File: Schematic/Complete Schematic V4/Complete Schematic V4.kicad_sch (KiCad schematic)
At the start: 62 parts

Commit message: New Update
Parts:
- removed R?: 50, symbol Device:R
- C1, C4: renamed from C?; value 270p -> (none)
- C10, C11, C12, C9: renamed from C?; value 0.22u -> (none)
- C13, C26, C27: renamed from C?; value 10u -> (none)
- C14, C15, C18, C21, C24, C25, C3, C5, C6: renamed from C?; value 0.1u -> (none)
- C16, C17, C7: renamed from C?; value 10n -> (none)
- C19, C20: renamed from C?; value 105p -> (none)
- C2: renamed from C?; value 560p -> (none)
- C22, C23: renamed from C?; value 100p -> (none)
- C8: renamed from C?; value 100n -> (none)
- J1: renamed from J?; footprint (none) -> Connector_Coaxial:BNC_Amphenol_B6252HB-NPP3G-50_Horizontal
- L1, L3: renamed from L?; value 750n -> (none)
- L2: renamed from L?; value 360n -> (none)
- R10, R11: renamed from R?; value 4.64k -> (none)
- R12, R13: renamed from R?; value 52.3k -> (none)
- R14, R15: renamed from R?; value 2.49k -> (none)
- R16, R17: renamed from R?; value 17.4k -> (none)
- R18, R19: renamed from R?; value 4.7k -> (none)
- R20, R21: renamed from R?; value 100 -> (none)
- R3: renamed from R?; value 10k -> (none)
- R4, R5, R6, R7: renamed from R?; value 200 -> (none)
- R8, R9: renamed from R?; value 22k -> (none)
- U1: renamed from U?; footprint Package_SO:MSOP-10_3x3mm_P0.5mm -> (none)
- U3, U4: renamed from U?; value OPAMP -> LT6231; footprint (none) -> Package_SO:SOIC-8_3.9x4.9mm_P1.27mm
- U5, U6: renamed from U?; value OPAMP -> LM4562MA; footprint (none) -> Package_SO:SOIC-8_3.9x4.9mm_P1.27mm
- gave numbers to parts that had none: 6
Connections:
- net at C1.2: now also J1.2 (Ext)
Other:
- moved on the sheet: C18

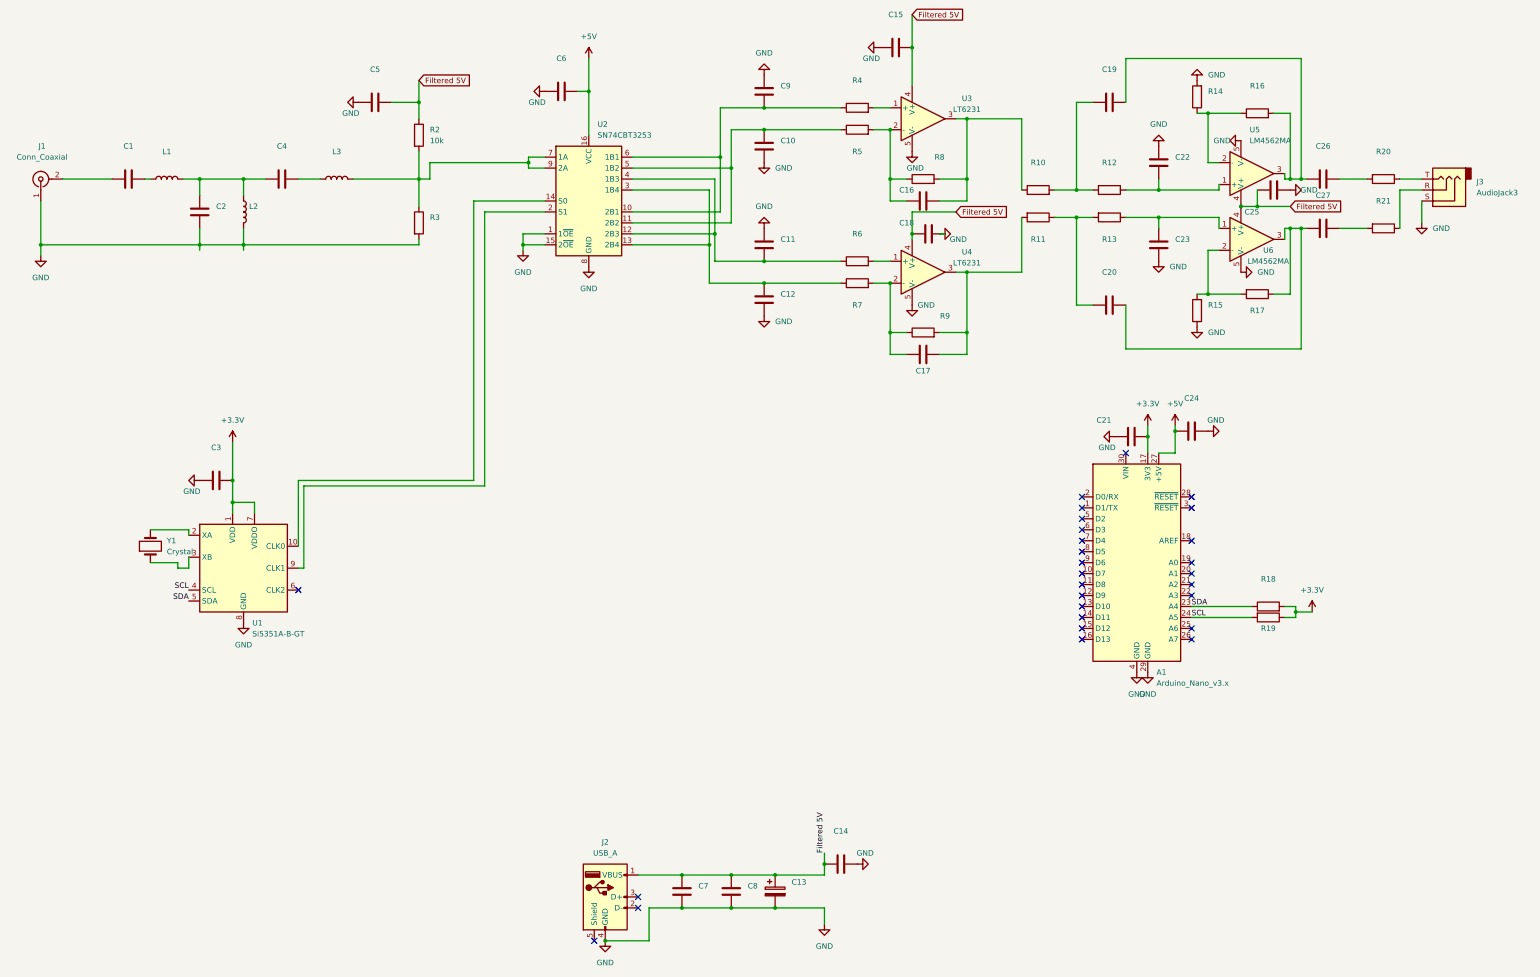
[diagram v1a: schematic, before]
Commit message: Schematic with all footprints for checking and the parts lists with the links
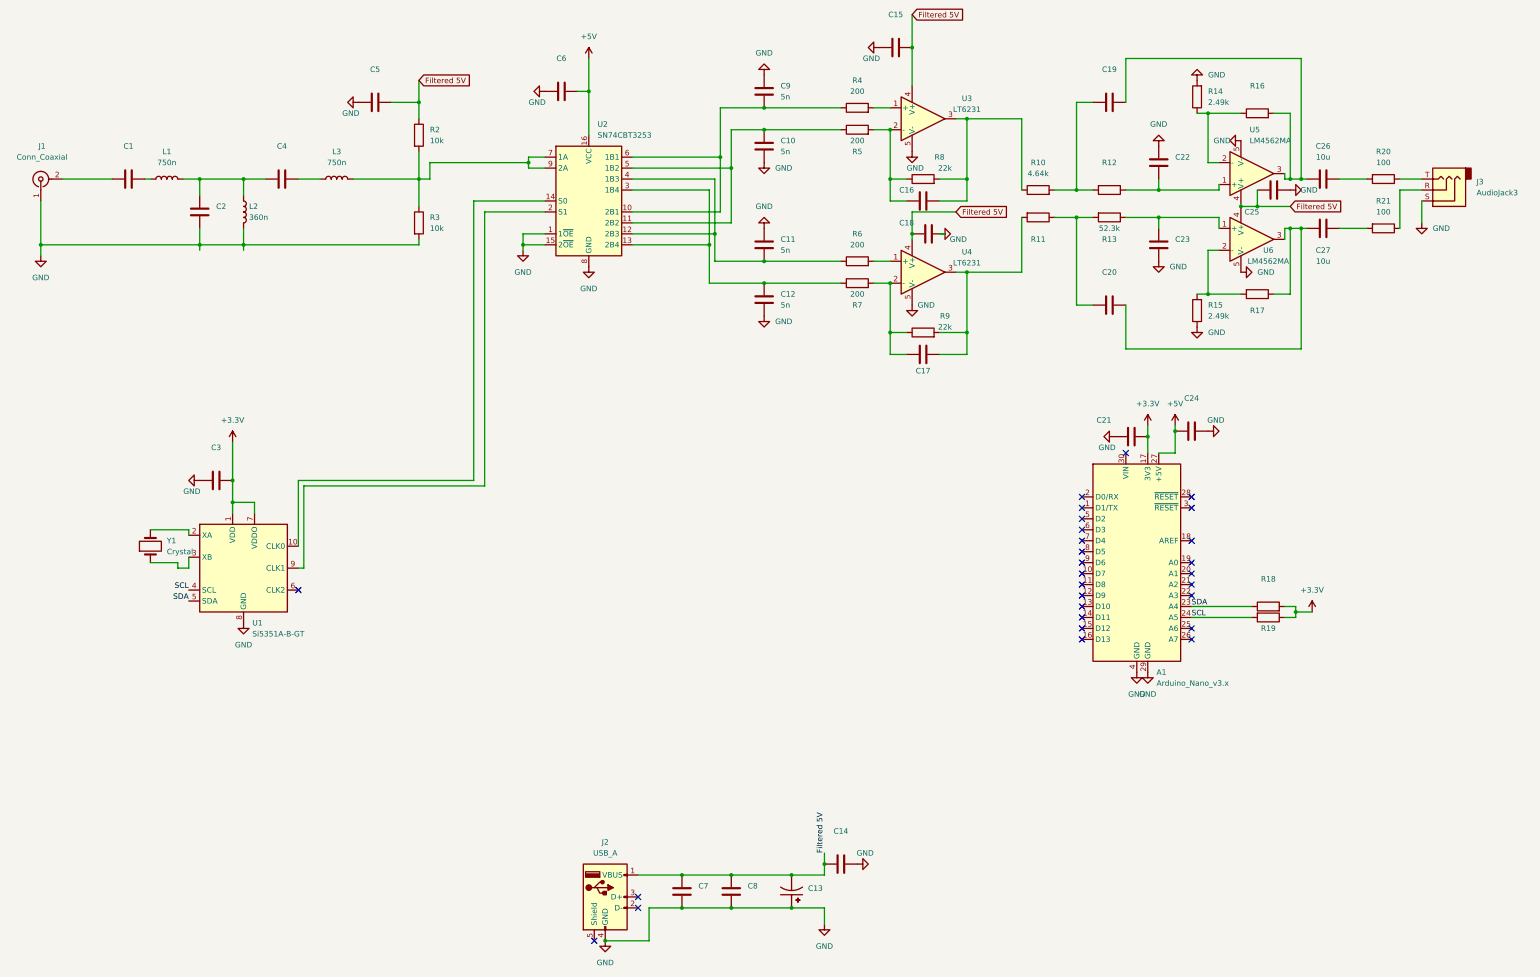
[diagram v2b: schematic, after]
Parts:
- removed C13: (no value), symbol Device:C_Polarized
- added C13: (no value), symbol EEEFK1C100R:EEEFK1C100R
- C10, C11, C12, C9: value (none) -> 5n
- C26, C27: value (none) -> 10u
- J3: footprint (none) -> Connector_Audio:Jack_3.5mm_CUI_SJ-3523-SMT_Horizontal
- L1: value (none) -> 750n
- L2: value (none) -> 360n
- L3: value (none) -> 750n; footprint (none) -> Inductor_SMD:L_0805_2012Metric
- R10: value (none) -> 4.64k
- R13: value (none) -> 52.3k
- R14, R15: value (none) -> 2.49k
- R20, R21: value (none) -> 100
- R3: value (none) -> 10k; footprint (none) -> Resistor_SMD:R_2512_6332Metric
- R4, R7: value (none) -> 200; footprint (none) -> Resistor_SMD:R_1206_3216Metric
- R5, R6: value (none) -> 200
- R8: value (none) -> 22k
- R9: value (none) -> 22k; footprint (none) -> Resistor_SMD:R_2512_6332Metric
- U1: footprint (none) -> Package_SO:MSOP-10_3x3mm_P0.5mm
- U2: footprint (none) -> Package_SO:SOIC-16_3.9x9.9mm_P1.27mm
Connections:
- net Filtered 5V: now also C13.2
- net GND: now also C13.1

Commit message: changes
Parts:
- removed Y1: Crystal, symbol Device:Crystal
- added TP1: (no value), symbol Connector:TestPoint
- added TP10, TP11, TP12, TP2, TP3, TP4, TP5, TP6, TP7, TP8, TP9: TestPoint, symbol Connector:TestPoint
- added Y1: (no value), symbol Device:Crystal_GND24_Small
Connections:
- net Filtered 5V: now also C13.1; no longer C13.2
- net GND: now also C13.2, Y1.2, Y1.4; no longer C13.1
- net at C1.2, J1.2 (Ext): now also TP1.1
- net at C26.1, R20.2: now also TP11.1
- net at C17.1, R11.2, R9.2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: now also TP8.1
- net at C16.1, R10.1, R8.2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: now also TP7.1
- net at C10.2, R5.1, U2.11 (2B2)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: now also TP4.1
- net at C12.2, R7.1, U2.13 (2B4)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: now also TP6.1
- net at C11.1, R6.1, U2.12 (2B3)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: now also TP5.1
- net at L3.2, R2.2, R3.1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: now also TP2.1
- net at C9.1, R4.1, U2.10 (2B1)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: now also TP3.1
- net at C19.1, R10.2, R12.2: now also TP9.1
- net at C20.1, R11.1, R13.2: now also TP10.1
- net at C27.1, R21.2: now also TP12.1
- net at U1.3 (XB): now also Y1.1
- net at U1.2 (XA): now also Y1.3
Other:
- moved on the sheet: C13

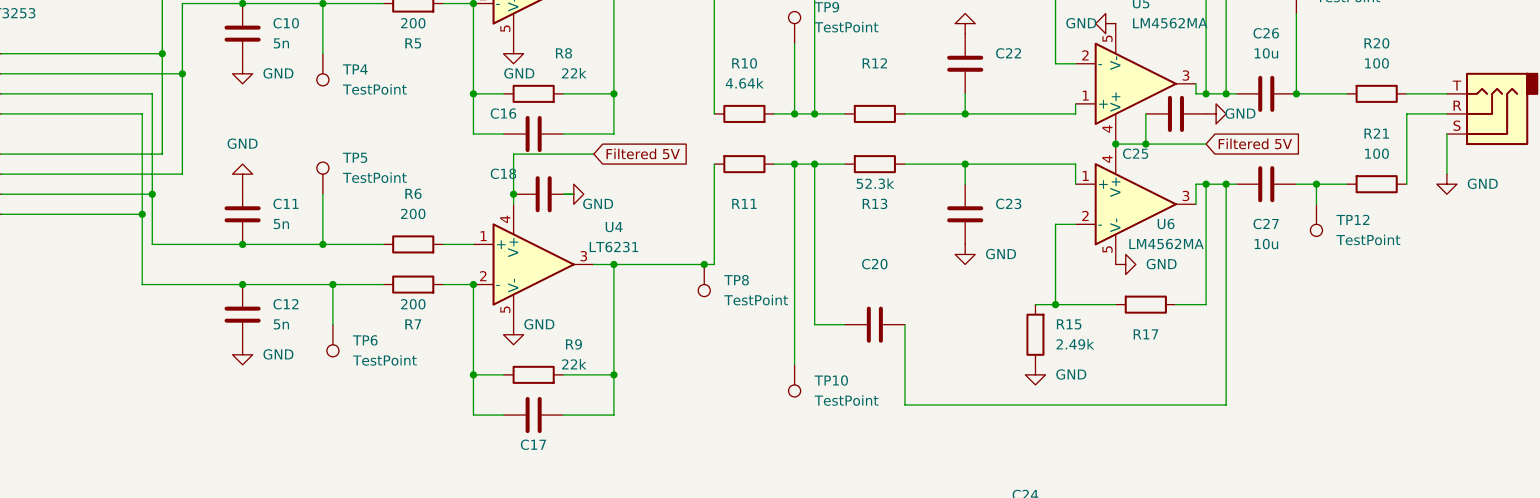
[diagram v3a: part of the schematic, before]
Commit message: Christian's PCB Work, But Josh's PCB Design is what we're using
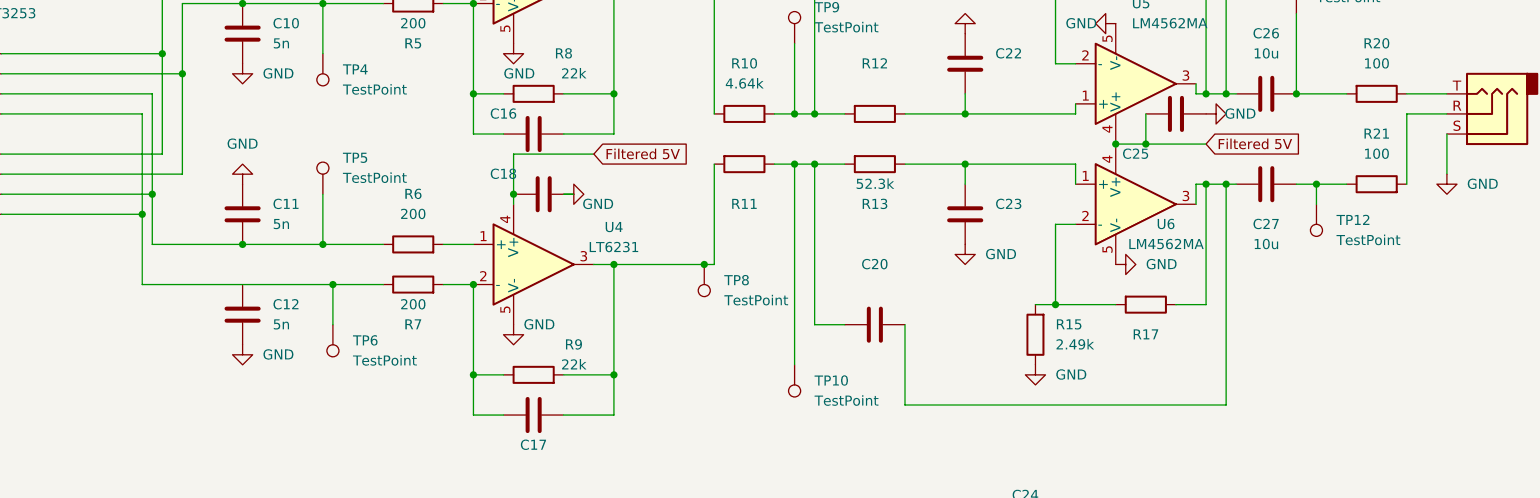
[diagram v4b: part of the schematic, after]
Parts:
- J1: footprint Connector_Coaxial:BNC_Amphenol_B6252HB-NPP3G-50_Horizontal -> (none)
- J3: footprint Connector_Audio:Jack_3.5mm_CUI_SJ-3523-SMT_Horizontal -> (none)
- U2: footprint Package_SO:SOIC-16_3.9x9.9mm_P1.27mm -> (none)
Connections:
- net GND: now also C12.2; no longer C12.1
- net at C27.1, TP12.1: now also R21.1; no longer R21.2
- net at R7.1, TP6.1, U2.13 (2B4)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: no longer C12.2
- net at J3.R: now also R21.2; no longer R21.1
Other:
- moved on the sheet: C12, R21
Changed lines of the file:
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@@
   (junction (at 205.74 77.47) (diameter 0) (color 0 0 0 0)
-  )
-  (junction (at 213.36 104.14) (diameter 0) (color 0 0 0 0)
   )
   (junction (at 219.71 241.3) (diameter 0) (color 0 0 0 0)
@@
     (stroke (width 0) (type default) (color 0 0 0 0))
   )
-  (wire (pts (xy 213.36 104.14) (xy 224.79 104.14))
-    (stroke (width 0) (type default) (color 0 0 0 0))
-  )
   (wire (pts (xy 247.65 49.53) (xy 247.65 58.42))
     (stroke (width 0) (type default) (color 0 0 0 0))
@@
     (stroke (width 0) (type default) (color 0 0 0 0))
   )
-  (wire (pts (xy 200.66 104.14) (xy 213.36 104.14))
+  (wire (pts (xy 200.66 104.14) (xy 224.79 104.14))
     (stroke (width 0) (type default) (color 0 0 0 0))
   )
@@
       (effects (font (size 1.27 1.27)) (justify left))
     )
-    (property "Footprint" "Package_SO:SOIC-16_3.9x9.9mm_P1.27mm" (id 2) (at 172.72 85.09 0)
+    (property "Footprint" "" (id 2) (at 172.72 85.09 0)
       (effects (font (size 1.27 1.27)) hide)
     )
@@
     (property "Reference" "J1" (id 0) (at 46.0132 72.39 90))
     (property "Value" "Conn_Coaxial" (id 1) (at 46.0132 74.93 90))
-    (property "Footprint" "Connector_Coaxial:BNC_Amphenol_B6252HB-NPP3G-50_Horizontal" (id 2) (at 45.72 80.01 0)
+    (property "Footprint" "" (id 2) (at 45.72 80.01 0)
       (effects (font (size 1.27 1.27)) hide)
     )
@@
     (pin "1")
   )
-  (symbol (lib_id "Device:C") (at 213.36 107.95 180) (unit 1)
+  (symbol (lib_id "Device:C") (at 213.36 107.95 0) (unit 1)
     (in_bom yes) (on_board yes) (fields_autoplaced)
     (property "Reference" "C12" (id 0) (at 217.17 106.6799 0)
-      (effects (font (size 1.27 1.27)) (justify right))
+      (effects (font (size 1.27 1.27)) (justify left))
     )
     (property "Value" "5n" (id 1) (at 217.17 109.2199 0)
-      (effects (font (size 1.27 1.27)) (justify right))
-    )
-    (property "Footprint" "" (id 2) (at 212.3948 104.14 0)
+      (effects (font (size 1.27 1.27)) (justify left))
+    )
+    (property "Footprint" "" (id 2) (at 214.3252 111.76 0)
       (effects (font (size 1.27 1.27)) hide)
     )
@@
     (pin "1")
   )
-  (symbol (lib_id "Device:R") (at 356.87 91.44 270) (unit 1)
+  (symbol (lib_id "Device:R") (at 356.87 91.44 90) (unit 1)
     (in_bom yes) (on_board yes) (fields_autoplaced)
     (property "Reference" "R21" (id 0) (at 356.87 85.09 90))
     (property "Value" "100" (id 1) (at 356.87 87.63 90))
-    (property "Footprint" "" (id 2) (at 356.87 89.662 90)
+    (property "Footprint" "" (id 2) (at 356.87 93.218 90)
       (effects (font (size 1.27 1.27)) hide)
     )
@@
       (effects (font (size 1.27 1.27)) (justify right))
     )
-    (property "Footprint" "Connector_Audio:Jack_3.5mm_CUI_SJ-3523-SMT_Horizontal" (id 2) (at 370.84 82.55 0)
-      (effects (font (size 1.27 1.27)) hide)
-    )
+    (property "Footprint" "" (id 2) (at 370.84 82.55 0)
+      (effects (font (size 1.27 1.27)) hide)
+    )
